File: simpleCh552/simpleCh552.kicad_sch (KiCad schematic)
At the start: 15 parts, among them J1 Conn_01x02_Pin, J2 left, J3 Conn_01x03_Pin, SW1 SW_SPST, U1 CH552G

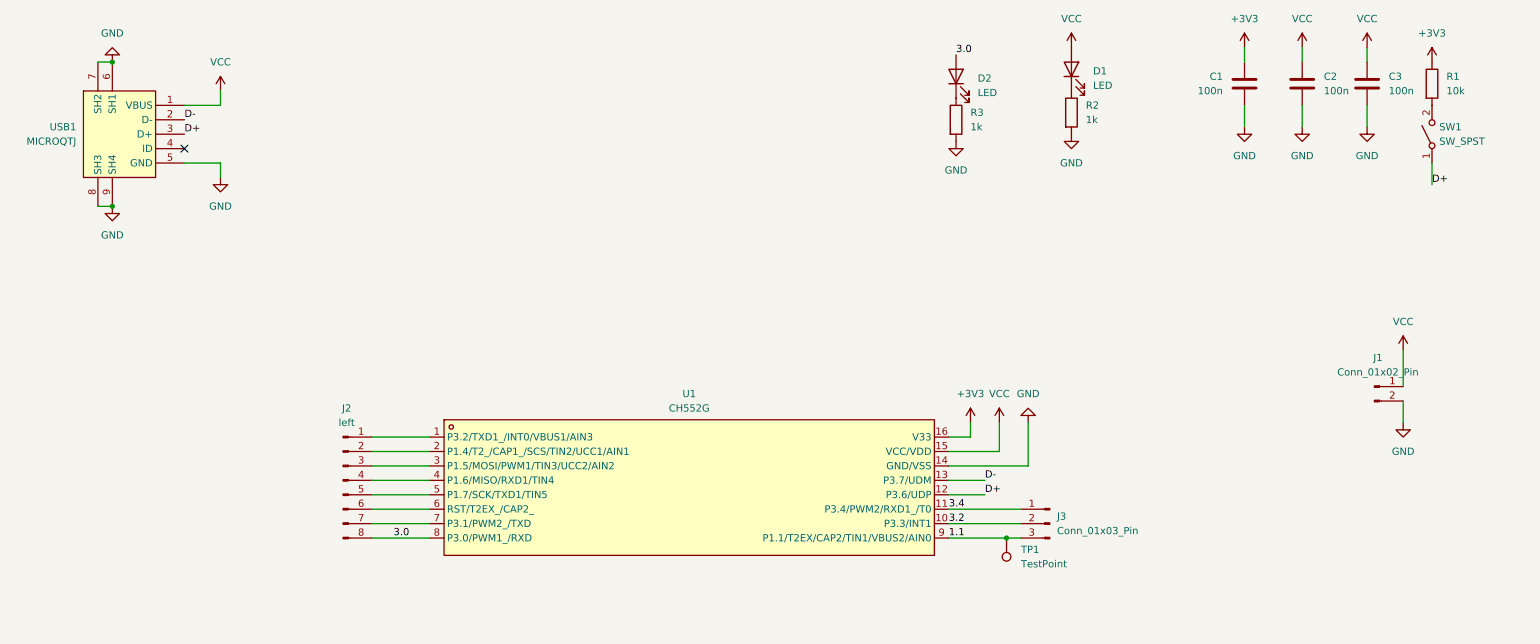
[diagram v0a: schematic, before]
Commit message: Updated with MicroUSB link
Microsub board ready V1
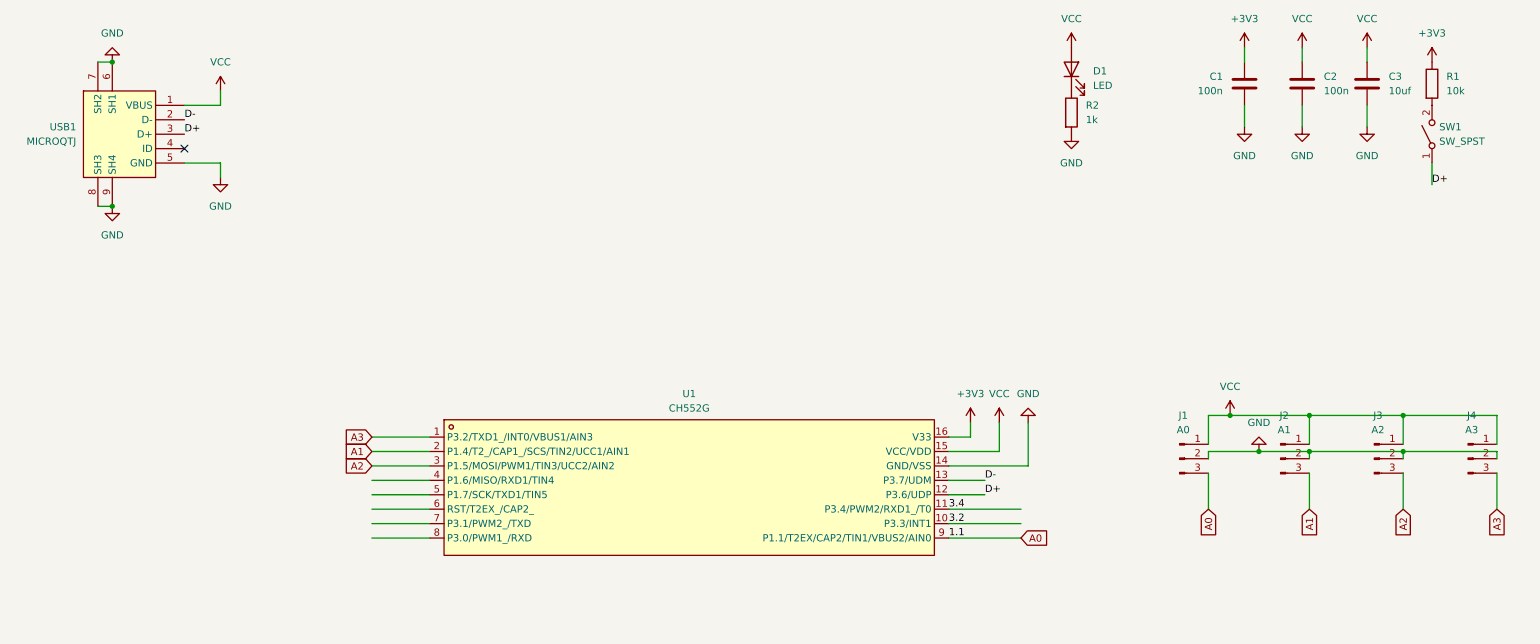
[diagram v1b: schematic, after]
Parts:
- removed D2: LED, LED_SMD:LED_1206_3216Metric, symbol Device:LED
- removed J1: Conn_01x02_Pin, Connector_PinHeader_2.00mm:PinHeader_2x01_P2.00mm_Vertical_SMD, symbol Connector:Conn_01x02_Pin
- removed J2: left, Connector_PinHeader_2.54mm:PinHeader_1x08_P2.54mm_Vertical, symbol Connector:Conn_01x08_Pin
- removed R3: 1k, Resistor_SMD:R_0603_1608Metric, symbol Device:R
- removed TP1: TestPoint, TestPoint:TestPoint_Keystone_5019_Miniature, symbol Connector:TestPoint
- added J1: A0, Connector_PinSocket_2.00mm:PinSocket_1x03_P2.00mm_Vertical, symbol Connector:Conn_01x03_Pin
- added J2: A1, Connector_PinSocket_2.00mm:PinSocket_1x03_P2.00mm_Vertical, symbol Connector:Conn_01x03_Pin
- added J4: A3, Connector_PinSocket_2.00mm:PinSocket_1x03_P2.00mm_Vertical, symbol Connector:Conn_01x03_Pin
- C3: value 100n -> 10uf; footprint Capacitor_SMD:C_0402_1005Metric -> Capacitor_SMD:C_0805_2012Metric
- J3: value Conn_01x03_Pin -> A2; footprint Connector_PinHeader_2.54mm:PinHeader_1x03_P2.54mm_Vertical -> Connector_PinSocket_2.00mm:PinSocket_1x03_P2.00mm_Vertical
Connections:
- net 3.2: no longer J3.2 (Pin_2)
- net 3.4: no longer J3.1 (Pin_1)
- net GND: now also J3.2 (Pin_2), J1.2 (Pin_2), J2.2 (Pin_2), J4.2 (Pin_2)
- net VCC: now also J3.1 (Pin_1), J1.1 (Pin_1), J2.1 (Pin_1), J4.1 (Pin_1)
- net A3: now reaches U1.1 (P3.2/TXD1_/INT0/VBUS1/AIN3)
- net A3: now also J4.3 (Pin_3)
- net A1: now reaches U1.2 (P1.4/T2_/CAP1_/SCS/TIN2/UCC1/AIN1)
- net A1: now also J2.3 (Pin_3)
- net A2: now reaches U1.3 (P1.5/MOSI/PWM1/TIN3/UCC2/AIN2)
- net A2: now also J3.3 (Pin_3)
- net 1.1 renamed A0
- net A0: now also J1.3 (Pin_3); no longer J3.3 (Pin_3)
- net 3.0: no longer names the net of U1.8 (P3.0/PWM1_/RXD)

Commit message: update
update
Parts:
- removed USB1: MICROQTJ, mylib:MICRO-USB-SMD_MICROQTJ-5P, symbol mylib:MICROQTJ
- added H1: MountingHole, MountingHole:MountingHole_2.1mm, symbol Mechanical:MountingHole
- added J5: Conn_01x04, Connector_PinSocket_2.54mm:PinSocket_1x04_P2.54mm_Vertical, symbol Connector_Generic:Conn_01x04
- R1, R2: footprint Resistor_SMD:R_0603_1608Metric -> Resistor_SMD:R_1206_3216Metric
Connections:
- net D+: now also J5.3 (Pin_3)
- net D-: now also J5.2 (Pin_2)
- net GND: now also J5.4 (Pin_4)
- net VCC: now also J5.1 (Pin_1)
- no-connect marks 1 -> 0

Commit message: update
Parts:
- removed H1: MountingHole, MountingHole:MountingHole_2.1mm, symbol Mechanical:MountingHole
- removed J1: A0, Connector_PinSocket_2.00mm:PinSocket_1x03_P2.00mm_Vertical, symbol Connector:Conn_01x03_Pin
- removed J2: A1, Connector_PinSocket_2.00mm:PinSocket_1x03_P2.00mm_Vertical, symbol Connector:Conn_01x03_Pin
- removed J3: A2, Connector_PinSocket_2.00mm:PinSocket_1x03_P2.00mm_Vertical, symbol Connector:Conn_01x03_Pin
- removed J4: A3, Connector_PinSocket_2.00mm:PinSocket_1x03_P2.00mm_Vertical, symbol Connector:Conn_01x03_Pin
- added J2, J3, J4: Conn_01x04, Connector_Wire:SolderWire-0.5sqmm_1x04_P4.6mm_D0.9mm_OD2.1mm, symbol Connector_Generic:Conn_01x04
- renumbered J5 to J1, R2 to R1, R1 to R2
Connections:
- net A0: now also J2.1 (Pin_1)
- net A1: now also J2.3 (Pin_3)
- net A2: now also J2.2 (Pin_2)
- net A3: now also J2.4 (Pin_4)
- net GND: now also J3.1 (Pin_1), J3.2 (Pin_2), J3.3 (Pin_3), J3.4 (Pin_4)
- net VCC: now also J4.1 (Pin_1), J4.2 (Pin_2), J4.3 (Pin_3), J4.4 (Pin_4)
- net 3.2: no longer names the net of U1.10 (P3.3/INT1)
- net 3.4: no longer names the net of U1.11 (P3.4/PWM2/RXD1_/T0)
- no-connect marks 0 -> 7
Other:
- moved on the sheet: C1, C2, C3, D1, J1, R1, R2, SW1, U1

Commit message: updated with pot
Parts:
- removed J2, J3, J4: Conn_01x04, Connector_Wire:SolderWire-0.5sqmm_1x04_P4.6mm_D0.9mm_OD2.1mm, symbol Connector_Generic:Conn_01x04
- added J5, J6: Conn_01x06, Connector_Wire:SolderWire-0.1sqmm_1x06_P3.6mm_D0.4mm_OD1mm, symbol Connector_Generic:Conn_01x06
- added RV1, RV2, RV3, RV4: pot1, Potentiometer_THT:Potentiometer_Omeg_PC16BU_Vertical, symbol Device:R_Potentiometer
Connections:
- net A0: now also J6.5 (Pin_5)
- net A1: now also J6.3 (Pin_3)
- net A2: now also J6.4 (Pin_4)
- net A3: now also J6.2 (Pin_2)
- net GND: now also J6.1 (Pin_1)
- net VCC: now also J6.6 (Pin_6)
- new net: J5.5 (Pin_5), RV4.2
- new net: J5.4 (Pin_4), RV3.2
- new net: J5.3 (Pin_3), RV2.2
- new net: J5.2 (Pin_2), RV1.2
- new net GND1: J5.6 (Pin_6), RV1.3, RV2.3, RV3.3, RV4.3
- new net VSS: J5.1 (Pin_1), RV1.1, RV2.1, RV3.1, RV4.1
